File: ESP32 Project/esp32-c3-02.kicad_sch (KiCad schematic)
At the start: 5 parts, among them J3 GSD090012SEU, U3 ESP32-C3-WROOM-02-H4, U4 CP2102N-Axx-xQFN20, U5 USBLC6-2SC6, U6 W25Q16JVSS

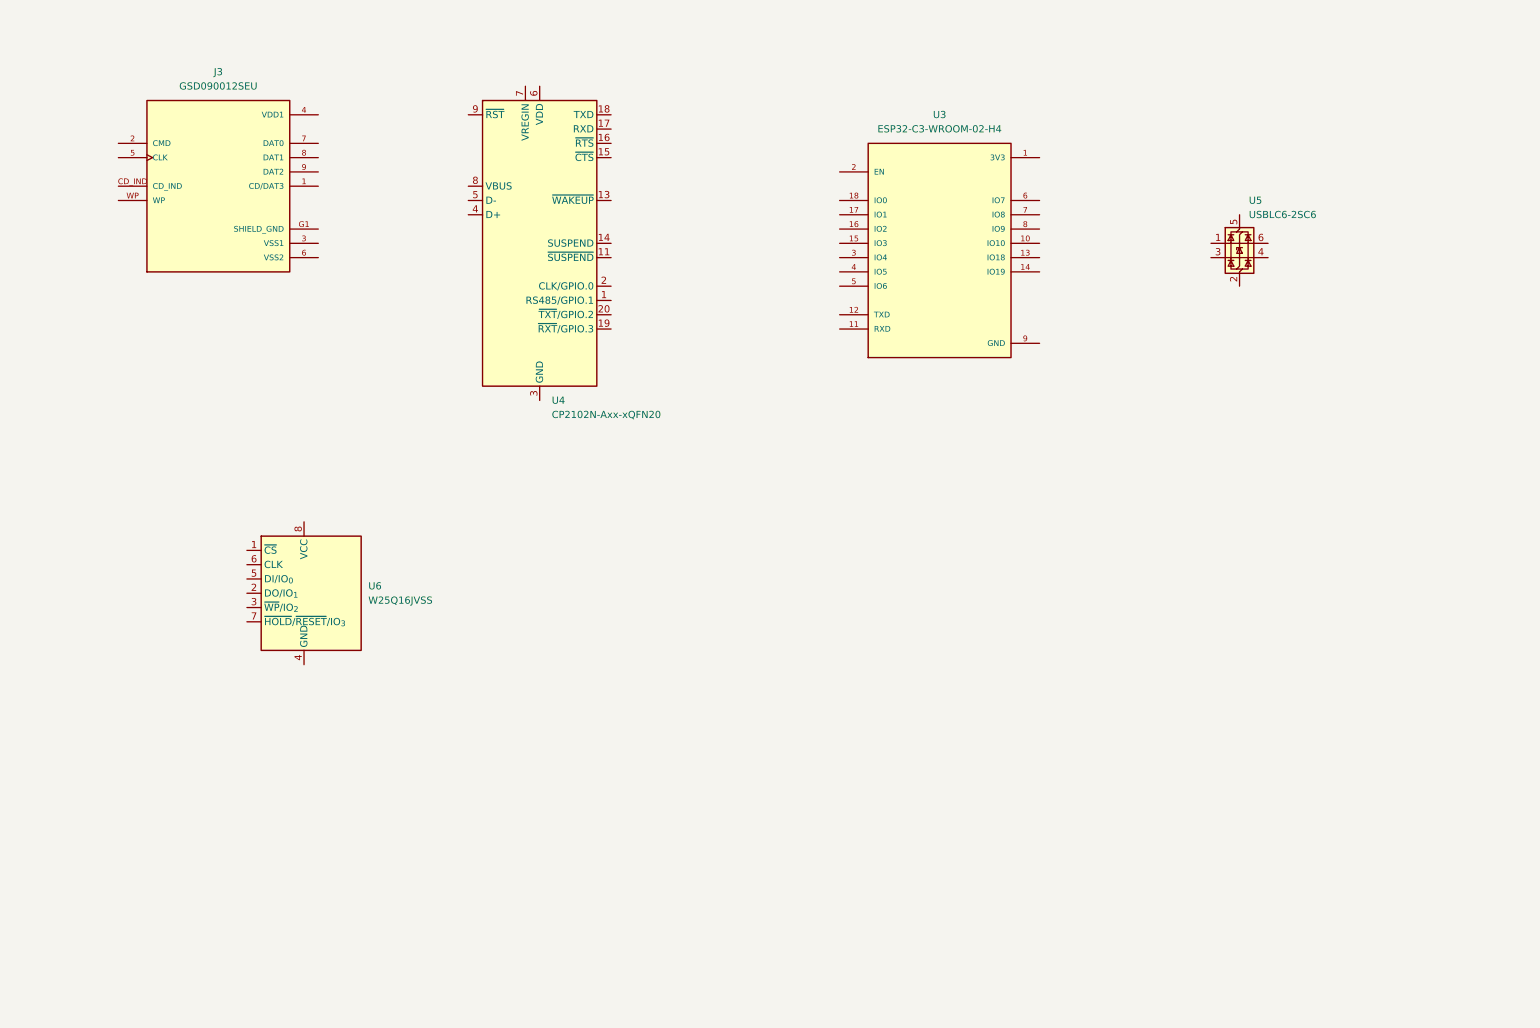
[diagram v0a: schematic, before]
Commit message: most of the schema is done , esp32 page is done
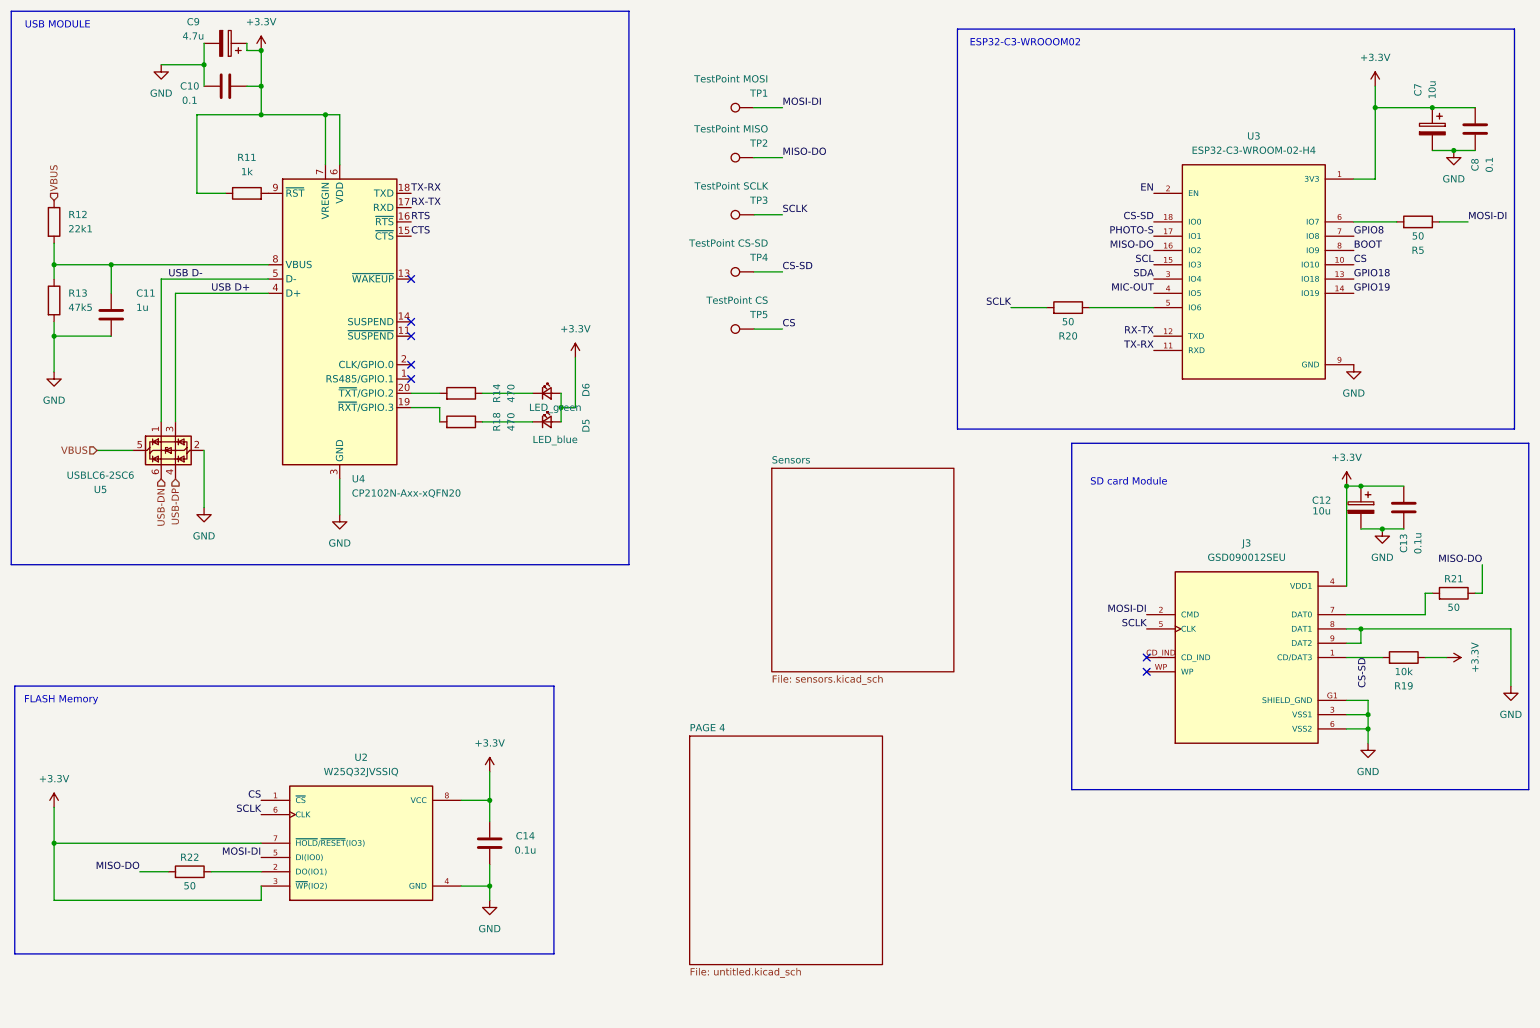
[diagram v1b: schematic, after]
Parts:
- removed U6: W25Q16JVSS, Package_SO:SOIC-8_5.3x5.3mm_P1.27mm, symbol Memory_Flash:W25Q16JVSS
- added C10, C8: 0.1, symbol Device:C
- added C11: 1u, symbol Device:C
- added C12, C7: 10u, symbol Device:C_Polarized
- added C13, C14: 0.1u, symbol Device:C
- added C9: 4.7u, symbol Device:C_Polarized
- added D5: LED_blue, LED_SMD:LED_0805_2012Metric_Pad1.15x1.40mm_HandSolder, symbol Device:LED_Small
- added D6: LED_green, LED_SMD:LED_0805_2012Metric_Pad1.15x1.40mm_HandSolder, symbol Device:LED_Small
- added R11: 1k, symbol Device:R
- added R12: 22k1, symbol Device:R
- added R13: 47k5, symbol Device:R
- added R14, R18: 470, symbol Device:R
- added R19: 10k, symbol Device:R
- added R20, R21, R22, R5: 50, symbol Device:R
- added TP1: TestPoint MOSI, symbol Connector:TestPoint
- added TP2: TestPoint MISO, symbol Connector:TestPoint
- added TP3: TestPoint SCLK, symbol Connector:TestPoint
- added TP4: TestPoint CS-SD, symbol Connector:TestPoint
- added TP5: TestPoint CS, symbol Connector:TestPoint
- added U2: W25Q32JVSSIQ, W25Q32JVSSIQ:SOIC127P790X216-8N, symbol W25Q32JVSSIQ:W25Q32JVSSIQ
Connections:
- net SHIELD_GND is gone; now on net GND: J3.G1 (SHIELD_GND), J3.G2 (SHIELD_GND), J3.G3 (SHIELD_GND), J3.G4 (SHIELD_GND)
- net GND: now also J3.3 (VSS1), J3.6 (VSS2), J3.8 (DAT1), J3.9 (DAT2), U4.12 (GND), U4.21 (GND), U4.3 (GND), U5.2 (GND), C10.2, C11.2, C12.2, C13.2, C14.1, C7.2, C8.2, C9.2, R13.2, U2.4 (GND)
- net CS-SD: now reaches J3.1 (CD/DAT3)
- net CS-SD: now also U3.18 (IO0), R19.2, TP4.1
- net MOSI-DI: now reaches J3.2 (CMD)
- net MOSI-DI: now also R5.1, TP1.1, U2.5 (DI(IO0))
- net +3.3V: now reaches J3.4 (VDD1)
- net +3.3V: now also U3.1 (3V3), U4.6 (VDD), U4.7 (VREGIN), C10.1, C12.1, C13.1, C14.2, C7.1, C8.1, C9.1, D5.2 (A), D6.2 (A), R11.1, R19.1, U2.3 (~{WP}(IO2)), U2.7 (~{HOLD}/~{RESET}(IO3)), U2.8 (VCC)
- net SCLK: now reaches J3.5 (CLK)
- net SCLK: now also R20.2, TP3.1, U2.6 (CLK)
- net at J3.7 (DAT0): now also R21.2
- net CTS: now reaches U4.15 (~{CTS})
- net RTS: now reaches U4.16 (~{RTS})
- net RX-TX: now reaches U4.17 (RXD)
- net RX-TX: now also U3.12 (TXD)
- net TX-RX: now reaches U4.18 (TXD)
- net TX-RX: now also U3.11 (RXD)
- net at U4.19 (~{RXT}/GPIO.3): now also R18.2
- net at U4.20 (~{TXT}/GPIO.2): now also R14.2
- net USB D+: now reaches U4.4 (D+)
- net USB D+: now also U5.3 (I/O2)
- net USB D-: now reaches U4.5 (D-)
- net USB D-: now also U5.1 (I/O1)
- net at U4.8 (VBUS): now also C11.1, R12.2, R13.1
- net at U4.9 (~{RST}): now also R11.2
- net CS: now reaches U3.10 (IO10)
- net CS: now also TP5.1, U2.1 (~{CS})
- net GPIO18: now reaches U3.13 (IO18)
- net GPIO19: now reaches U3.14 (IO19)
- net SCL: now reaches U3.15 (IO3)
- net MISO-DO: now reaches U3.16 (IO2)
- net MISO-DO: now also R21.1, R22.2, TP2.1
- net PHOTO-S: now reaches U3.17 (IO1)
- net EN: now reaches U3.2 (EN)
- net SDA: now reaches U3.3 (IO4)
- net MIC-OUT: now reaches U3.4 (IO5)
- net at U3.5 (IO6): now also R20.1
- net at U3.6 (IO7): now also R5.2
- net GPIO8: now reaches U3.7 (IO8)
- net BOOT: now reaches U3.8 (IO9)
- net USB-DP: now reaches U5.4 (I/O2)
- net VBUS: now reaches U5.5 (VBUS)
- net VBUS: now also R12.1
- net USB-DN: now reaches U5.6 (I/O1)
- new net: R22.1, U2.2 (DO(IO1))
- new net: D6.1 (K), R14.1
- new net: D5.1 (K), R18.1
- no-connect marks 0 -> 7
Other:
- added sheet PAGE 4 (untitled.kicad_sch)
- added sheet Sensors (sensors.kicad_sch)
- note added: "ESP32-C3-WROOOM02"
- note added: "FLASH Memory"
- note added: "SD card Module"
- note added: "USB MODULE"
- moved on the sheet: J3, U3, U4, U5

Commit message: we are at edge of work , almost complete and now going for the pcb design and routign
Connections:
- net PHOTO-S renamed PHOTO-C
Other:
- sheet Sensors ports: added Mic_OUT, PHOTO C, SCL, SDA; removed none
- note added: "Page 4 contains the subcircuits for the boot and en buttons, and the headers for the gpio and i2c pins."
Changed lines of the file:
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@@
 		)
 	)
+	(text "Page 4 contains the subcircuits for the boot and en buttons, \nand the headers for the gpio and i2c pins.\n"
+		(exclude_from_sim no)
+		(at 144.78 191.77 0)
+		(effects
+			(font
+				(size 1.27 1.27)
+			)
+			(justify bottom)
+		)
+	)
 	(text "ESP32-C3-WROOOM02"
 		(exclude_from_sim no)
@@
 		)
 	)
+	(label "MIC-OUT"
+		(at 181.61 101.6 0)
+		(effects
+			(font
+				(size 1.27 1.27)
+			)
+			(justify left bottom)
+		)
+	)
+	(label "SDA"
+		(at 181.61 118.11 0)
+		(effects
+			(font
+				(size 1.27 1.27)
+			)
+			(justify left bottom)
+		)
+	)
 	(label "BOOT"
 		(at 252.73 55.88 0)
@@
 		)
 	)
-	(label "PHOTO-S"
+	(label "PHOTO-C"
 		(at 217.17 53.34 180)
 		(effects
@@
 		)
 	)
+	(label "SCL"
+		(at 181.61 113.03 0)
+		(effects
+			(font
+				(size 1.27 1.27)
+			)
+			(justify left bottom)
+		)
+	)
 	(label "RTS"
 		(at 85.09 50.8 0)
@@
 		)
 	)
+	(label "PHOTO-C"
+		(at 181.61 106.68 0)
+		(effects
+			(font
+				(size 1.27 1.27)
+			)
+			(justify left bottom)
+		)
+	)
 	(label "MISO-DO"
 		(at 151.13 39.37 0)
@@
 			)
 		)
+		(pin "Mic_OUT" output
+			(at 181.61 101.6 0)
+			(effects
+				(font
+					(size 1.27 1.27)
+				)
+				(justify right)
+			)
+		)
+		(pin "PHOTO C" output
+			(at 181.61 106.68 0)
+			(effects
+				(font
+					(size 1.27 1.27)
+				)
+				(justify right)
+			)
+		)
+		(pin "SCL" input
+			(at 181.61 113.03 0)
+			(effects
+				(font
+					(size 1.27 1.27)
+				)
+				(justify right)
+			)
+		)
+		(pin "SDA" input
+			(at 181.61 118.11 0)
+			(effects
+				(font
+					(size 1.27 1.27)
+				)
+				(justify right)
+			)
+		)
 		(instances
 			(project "ESP32 Project"
@@
 	)
 	(sheet
-		(at 134.62 142.24)
+		(at 128.27 143.51)
 		(size 34.29 40.64)
 		(exclude_from_sim no)
@@
 		)
 		(property "Sheetname" "PAGE 4"
-			(at 134.62 141.5284 0)
+			(at 128.27 142.7984 0)
 			(show_name no)
 			(do_not_autoplace no)
@@
 		)
 		(property "Sheetfile" "untitled.kicad_sch"
-			(at 134.62 183.4646 0)
+			(at 128.27 184.7346 0)
 			(show_name no)
 			(do_not_autoplace no)

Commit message: schema is done
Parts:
- C10, C11, C13, C14, C8: footprint (none) -> Capacitor_SMD:C_0805_2012Metric
- C12, C7, C9: footprint (none) -> Capacitor_SMD:CP_Elec_4x3
- R11, R12, R13, R14, R18, R19, R20, R22: footprint (none) -> Resistor_SMD:R_0805_2012Metric
- R15: renamed from R5; footprint (none) -> Resistor_SMD:R_0805_2012Metric
- R16: renamed from R21; footprint (none) -> Resistor_SMD:R_0805_2012Metric
- TP1, TP2, TP3, TP4, TP5: footprint (none) -> TestPoint:TestPoint_Pad_D1.0mm
- U3: footprint ESP32-C3-WROOM-02-H4:MODULE_ESP32-C3-WROOM-02-H4 -> Esp32 c3 wroom 02:MODULE_ESP32-C3-WROOM-02-H4
- U4: footprint Package_DFN_QFN:SiliconLabs_QFN-20-1EP_3x3mm_P0.5mm -> Package_DFN_QFN:QFN-20-1EP_3x3mm_P0.45mm_EP1.6x1.6mm
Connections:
- net CTS renamed DTR
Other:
- sheet PAGE 4 ports: added DTR, EN, GPIO18, GPIO19, GPIO8, IO0 / BOOT, RTS, SCL, SDA; removed none

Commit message: something done lmao
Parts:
- C12, C7, C9: footprint Capacitor_SMD:CP_Elec_4x3 -> Capacitor_SMD:C_Elec_5x5.4
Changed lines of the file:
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@@
 			)
 		)
-		(property "Footprint" "Capacitor_SMD:CP_Elec_4x3"
+		(property "Footprint" "Capacitor_SMD:C_Elec_5x5.4"
 			(at 48.26 18.0848 0)
 			(hide yes)
@@
 			)
 		)
-		(property "Footprint" "Capacitor_SMD:CP_Elec_4x3"
+		(property "Footprint" "Capacitor_SMD:C_Elec_5x5.4"
 			(at 253.0348 105.41 0)
 			(hide yes)
@@
 			)
 		)
-		(property "Footprint" "Capacitor_SMD:CP_Elec_4x3"
+		(property "Footprint" "Capacitor_SMD:C_Elec_5x5.4"
 			(at 265.7348 38.1 0)
 			(hide yes)

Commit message: pcb ont he way tomoroow
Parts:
- C12, C7, C9: footprint Capacitor_SMD:C_Elec_5x5.4 -> Capacitor_Tantalum_SMD:CP_EIA-6032-28_Kemet-C
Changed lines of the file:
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@@
 			)
 		)
-		(property "Footprint" "Capacitor_SMD:C_Elec_5x5.4"
+		(property "Footprint" "Capacitor_Tantalum_SMD:CP_EIA-6032-28_Kemet-C"
 			(at 48.26 18.0848 0)
 			(hide yes)
@@
 			)
 		)
-		(property "Footprint" "Capacitor_SMD:C_Elec_5x5.4"
+		(property "Footprint" "Capacitor_Tantalum_SMD:CP_EIA-6032-28_Kemet-C"
 			(at 253.0348 105.41 0)
 			(hide yes)
@@
 			)
 		)
-		(property "Footprint" "Capacitor_SMD:C_Elec_5x5.4"
+		(property "Footprint" "Capacitor_Tantalum_SMD:CP_EIA-6032-28_Kemet-C"
 			(at 265.7348 38.1 0)
 			(hide yes)

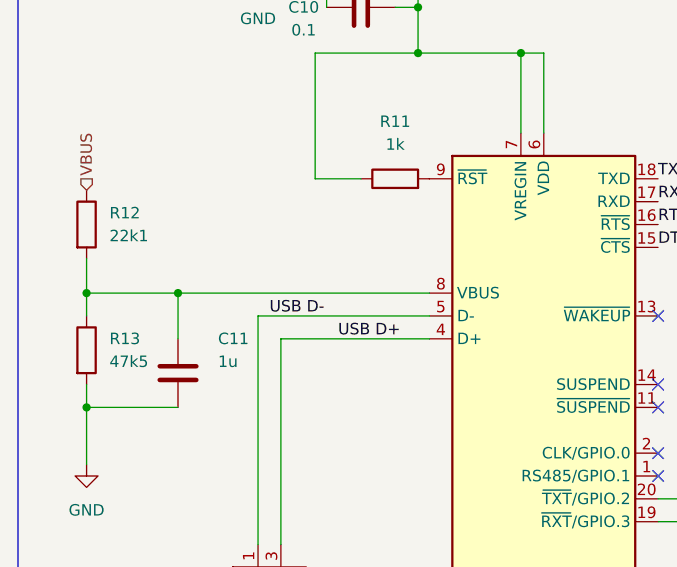
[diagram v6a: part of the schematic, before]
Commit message: pcb done and some 3d models aadd
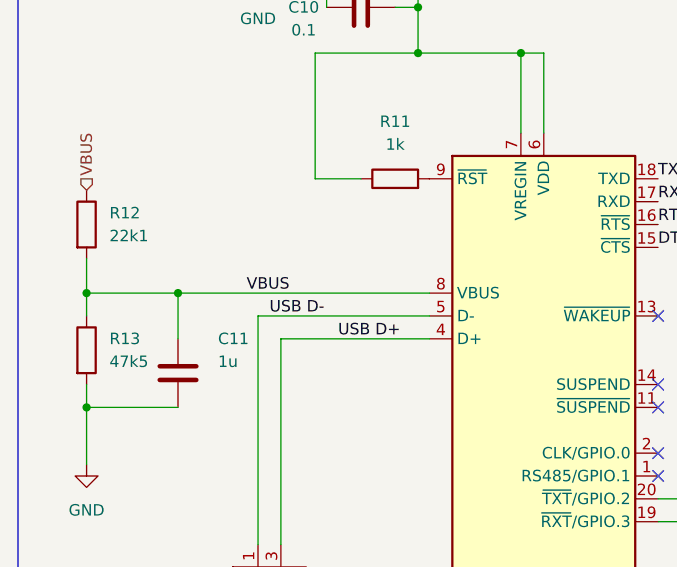
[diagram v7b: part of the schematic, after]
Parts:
- C12, C7, C9: footprint Capacitor_Tantalum_SMD:CP_EIA-6032-28_Kemet-C -> Capacitor_Tantalum_SMD:CP_EIA-3216-12_Kemet-S
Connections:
- net VBUS: now also C11.1, R12.2, R13.1, U4.8 (VBUS)
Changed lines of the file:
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@@
 		)
 	)
+	(label "VBUS"
+		(at 39.37 58.42 0)
+		(effects
+			(font
+				(size 1.27 1.27)
+			)
+			(justify left bottom)
+		)
+	)
 	(label "USB D+"
 		(at 49.53 63.5 0)
@@
 			)
 		)
-		(property "Footprint" "Capacitor_Tantalum_SMD:CP_EIA-6032-28_Kemet-C"
+		(property "Footprint" "Capacitor_Tantalum_SMD:CP_EIA-3216-12_Kemet-S"
 			(at 48.26 18.0848 0)
 			(hide yes)
@@
 			)
 		)
-		(property "Footprint" "Capacitor_Tantalum_SMD:CP_EIA-6032-28_Kemet-C"
+		(property "Footprint" "Capacitor_Tantalum_SMD:CP_EIA-3216-12_Kemet-S"
 			(at 253.0348 105.41 0)
 			(hide yes)
@@
 			)
 		)
-		(property "Footprint" "Capacitor_Tantalum_SMD:CP_EIA-6032-28_Kemet-C"
+		(property "Footprint" "Capacitor_Tantalum_SMD:CP_EIA-3216-12_Kemet-S"
 			(at 265.7348 38.1 0)
 			(hide yes)

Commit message: tomorrow is gonna be complete
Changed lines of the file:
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@@
+	)
+	(junction
+		(at 58.42 29.21)
+		(diameter 0)
+		(color 0 0 0 0)
 	)
 	(junction
@@
 	)
 	(junction
-		(at 58.42 31.75)
-		(diameter 0)
-		(color 0 0 0 0)
-	)
-	(junction
 		(at 21.59 161.29)
 		(diameter 0)
@@
 	(wire
 		(pts
-			(xy 58.42 26.67) (xy 58.42 31.75)
+			(xy 58.42 26.67) (xy 58.42 29.21)
 		)
 		(stroke
@@
 	(wire
 		(pts
-			(xy 46.99 31.75) (xy 58.42 31.75)
-		)
-		(stroke
-			(width 0)
-			(type default)
-		)
-	)
-	(wire
-		(pts
 			(xy 58.42 171.45) (xy 58.42 168.91)
 		)
@@
 	(wire
 		(pts
+			(xy 58.42 29.21) (xy 58.42 31.75)
+		)
+		(stroke
+			(width 0)
+			(type default)
+		)
+	)
+	(wire
+		(pts
 			(xy 254 123.19) (xy 280.67 123.19)
 		)
@@
 	(wire
 		(pts
+			(xy 46.99 31.75) (xy 55.88 31.75)
+		)
+		(stroke
+			(width 0)
+			(type default)
+		)
+	)
+	(wire
+		(pts
+			(xy 55.88 31.75) (xy 55.88 29.21)
+		)
+		(stroke
+			(width 0)
+			(type default)
+		)
+	)
+	(wire
+		(pts
 			(xy 21.59 154.94) (xy 21.59 161.29)
 		)
@@
 		)
 		(stroke
+			(width 0)
+			(type default)
+		)
+	)
+	(wire
+		(pts
+			(xy 55.88 29.21) (xy 58.42 29.21)
+		)
+		(stroke
